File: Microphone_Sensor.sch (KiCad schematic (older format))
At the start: 26 parts, among them J7 JST-GH, U4 TS472

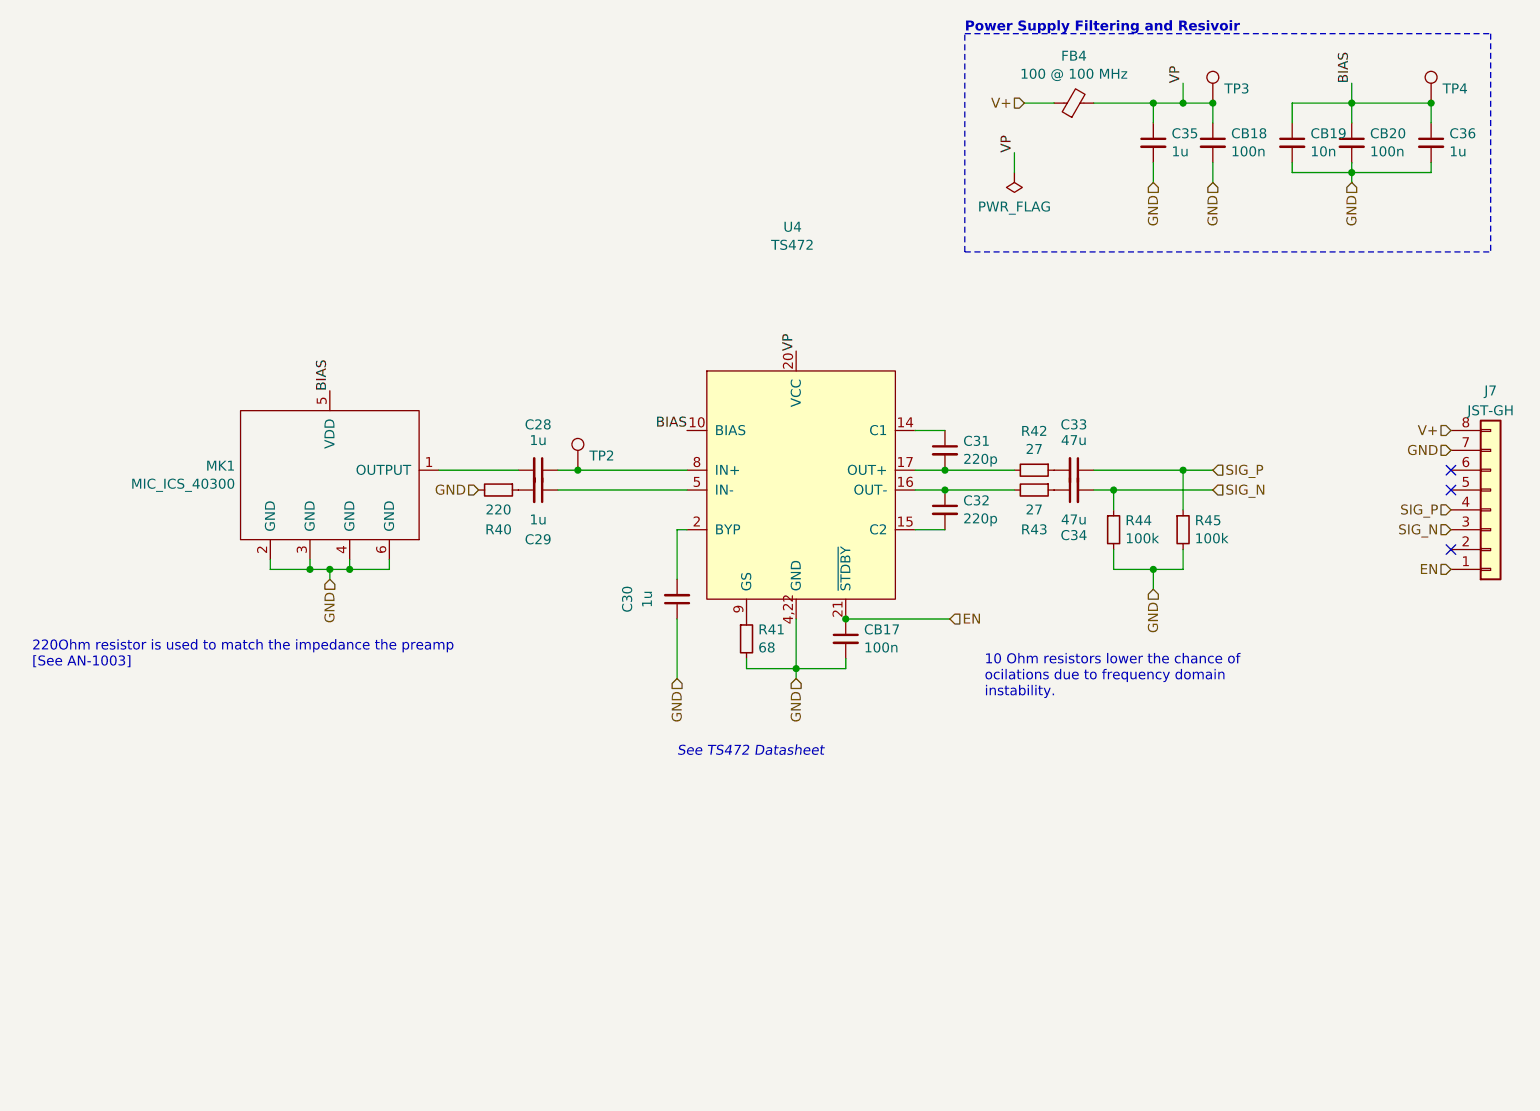
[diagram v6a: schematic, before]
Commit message: Change Mic Preamp
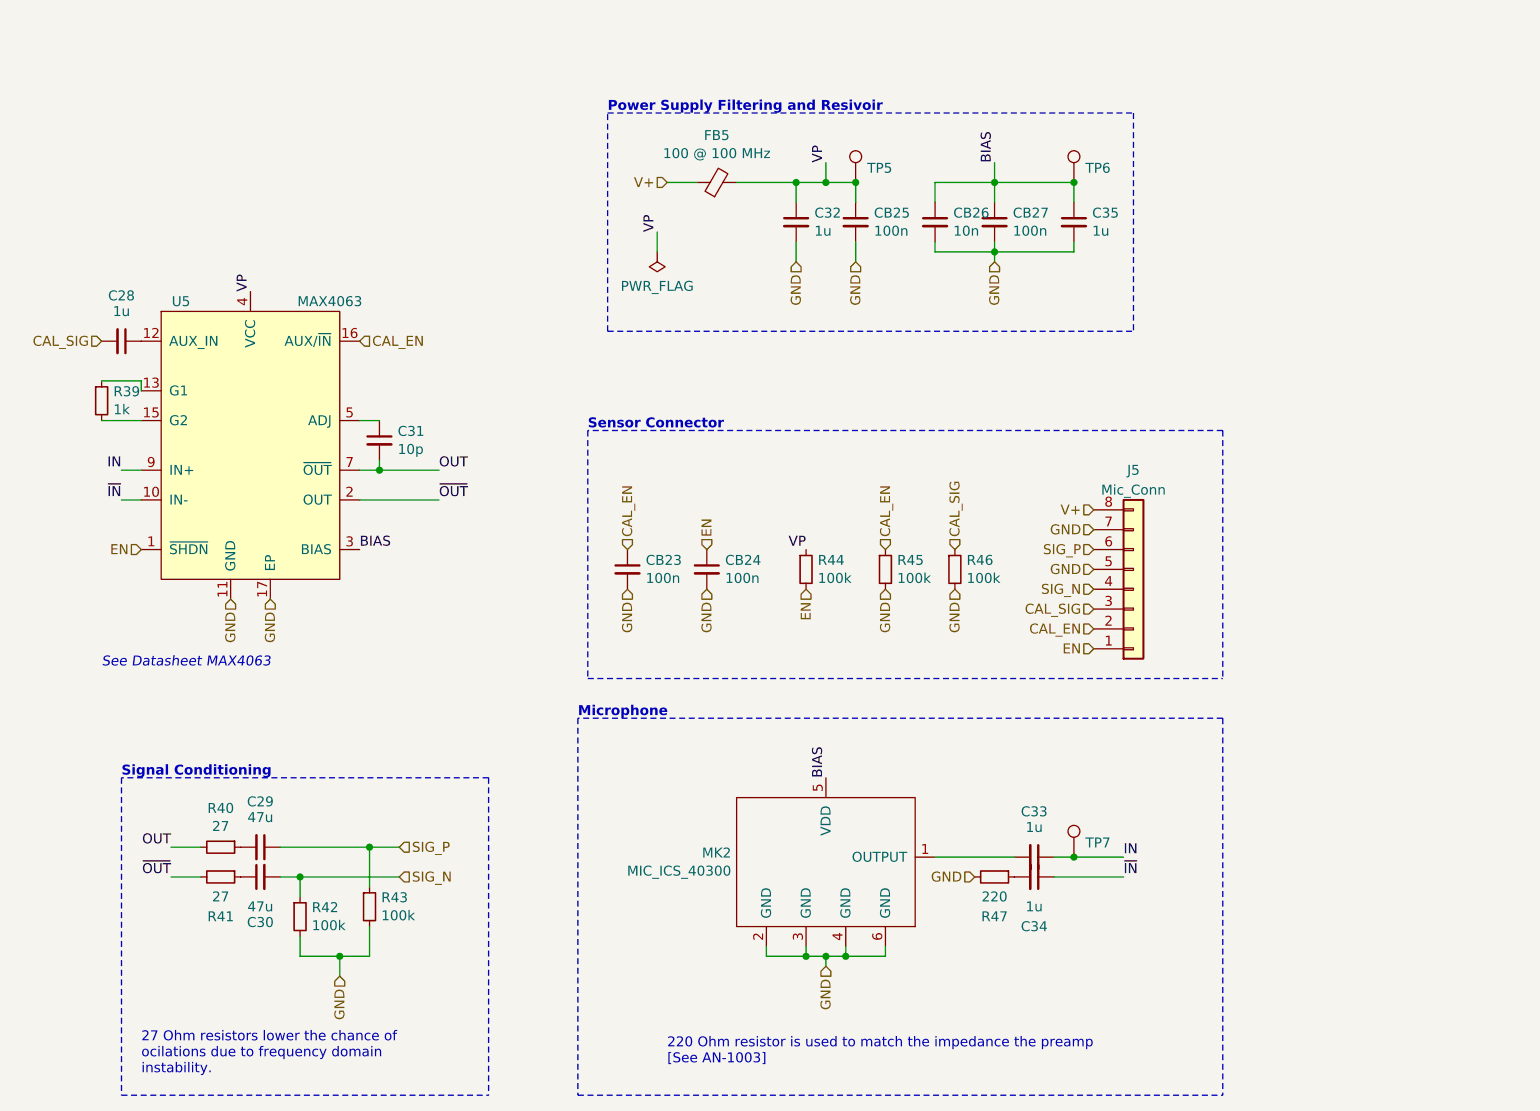
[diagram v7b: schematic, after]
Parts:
- removed C30: 1u, Capacitor_SMD:C_0603_1608Metric_Pad1.05x0.95mm_HandSolder, symbol Device:C_Small
- removed C31, C32: 220p, Capacitor_SMD:C_0603_1608Metric_Pad1.05x0.95mm_HandSolder, symbol Device:C_Small
- removed CB17: 100n, Capacitor_SMD:C_0603_1608Metric_Pad1.05x0.95mm_HandSolder, symbol Device:C_Small
- removed R41: 68, Resistor_SMD:R_0603_1608Metric_Pad1.05x0.95mm_HandSolder, symbol Device:R_Small
- removed U4: TS472, Package_DFN_QFN:VQFN-24-1EP_4x4mm_P0.5mm_EP2.45x2.45mm_ThermalVias, symbol grootvoet:TS472
- added C20: 1u, Capacitor_SMD:C_0603_1608Metric_Pad1.05x0.95mm_HandSolder, symbol Device:C_Small
- added C23: 10p, Capacitor_SMD:C_0603_1608Metric_Pad1.05x0.95mm_HandSolder, symbol Device:C_Small
- added CB18, CB19: 100n, Capacitor_SMD:C_0603_1608Metric_Pad1.05x0.95mm_HandSolder, symbol Device:C_Small
- added R30: 1k, Resistor_SMD:R_0603_1608Metric_Pad1.05x0.95mm_HandSolder, symbol Device:R_Small
- added R35, R36, R37: 100k, Resistor_SMD:R_0603_1608Metric_Pad1.05x0.95mm_HandSolder, symbol Device:R_Small
- added U4: MAX4063, grootvoet:TQFN-16-T1644++4, symbol grootvoet:MAX4063
- CB20: renamed from CB18; MPN (none) -> C0603C104M5RACTU; Mfr. (none) -> KEMET
- CB21: renamed from CB19; MPN (none) -> C0603C103J5RACTU; Mfr. (none) -> KEMET
- CB22: renamed from CB20; MPN (none) -> C0603C104M5RACTU; Mfr. (none) -> KEMET
- FB4: MPN BLM18KG101TZ1D -> BLM18EG101TZ1D
- J4: renamed from J7; value JST-GH -> Mic_Conn
- MK1: MPN (none) -> ICS-40300; Mfr. (none) -> TDK InvenSense
- R31: renamed from R42; MPN (none) -> RC0603FR-0727RL; Mfr. (none) -> Yageo
- R32: renamed from R43; MPN (none) -> RC0603FR-0727RL; Mfr. (none) -> Yageo
- R38: renamed from R40; MFN ERJ-3RBD2200V -> (none); MPN (none) -> ERJ-3RBD2200V
- renumbered C33 to C21, C34 to C22, C35 to C24, C28 to C25, C29 to C26, C36 to C27, R44 to R33, R45 to R34, TP3 to TP2, TP4 to TP3, TP2 to TP4
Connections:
- net BIAS: now also U4.3 (BIAS)
- net EN: now also CB19.1, R35.2, U4.1 (~SHDN)
- net GND: now also J4.5 (Pin_5), CB18.2, CB19.2, R36.2, R37.2, U4.11 (GND), U4.17 (EP)
- net SIG_N: now also J4.4 (Pin_4); no longer J4.3 (Pin_3)
- net SIG_P: now also J4.6 (Pin_6); no longer J4.4 (Pin_4)
- net VP: now also R35.1, U4.4 (VCC)
- net ~OUT: now reaches R32.2
- net ~OUT: now also U4.2 (OUT)
- net OUT: now reaches R31.2
- net OUT: now also C23.2, U4.7 (~OUT)
- net ~IN: now reaches C26.1
- net ~IN: now also U4.10 (IN-)
- net IN: now reaches C25.1, TP4.1
- net IN: now also U4.9 (IN+)
- net CAL_EN: now reaches J4.2 (Pin_2)
- net CAL_EN: now also CB18.1, R36.1, U4.16 (AUX/~IN)
- new net: C20.1, U4.12 (AUX_IN)
- new net: R30.1, U4.13 (G1)
- new net: R30.2, U4.15 (G2)
- new net: C23.1, U4.5 (ADJ)
- new net CAL_SIG: C20.2, J4.3 (Pin_3), R37.1
- no-connect marks 3 -> 0
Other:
- note added: "220 Ohm resistor is used to match the impedance the preamp\n[See AN-1003]"
- note added: "27 Ohm resistors lower the chance of \nocilations due to frequency domain \ninstability."
- note added: "Microphone"
- note added: "See Datasheet MAX4063"
- note added: "Sensor Connector"
- note added: "Signal Conditioning"
- note removed: "10 Ohm resistors lower the chance of \nocilations due to frequency domain \ninstability."
- note removed: "220Ohm resistor is used to match the impedance the preamp\n[See AN-1003]"
- note removed: "See TS472 Datasheet"
- moved on the sheet: C29, C30, C32, C33, C34, C35, CB25, CB26, CB27, FB5, J5, MK2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

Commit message: Fix BOM ref
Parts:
- J4: MPN (none) -> 53047-0810; Mfr. (none) -> Molex
- U4: MPN (none) -> MAX4063ETE+T; Mfr. (none) -> Maxim Integrated
